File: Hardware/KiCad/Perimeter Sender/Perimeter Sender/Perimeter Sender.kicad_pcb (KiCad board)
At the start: 2 copper layers, 133.7 x 77.9 mm, 29 parts, among them J1 Conn_01x02, J2 Conn_01x02, J3 Conn_02x05_Row_Letter_Last, U1 AVR128DA48x-xPT, U2 INA233, U3 WeMos_D1_mini, U4 L298N, U5 TSR_1-2450, Y1 32.768kHz

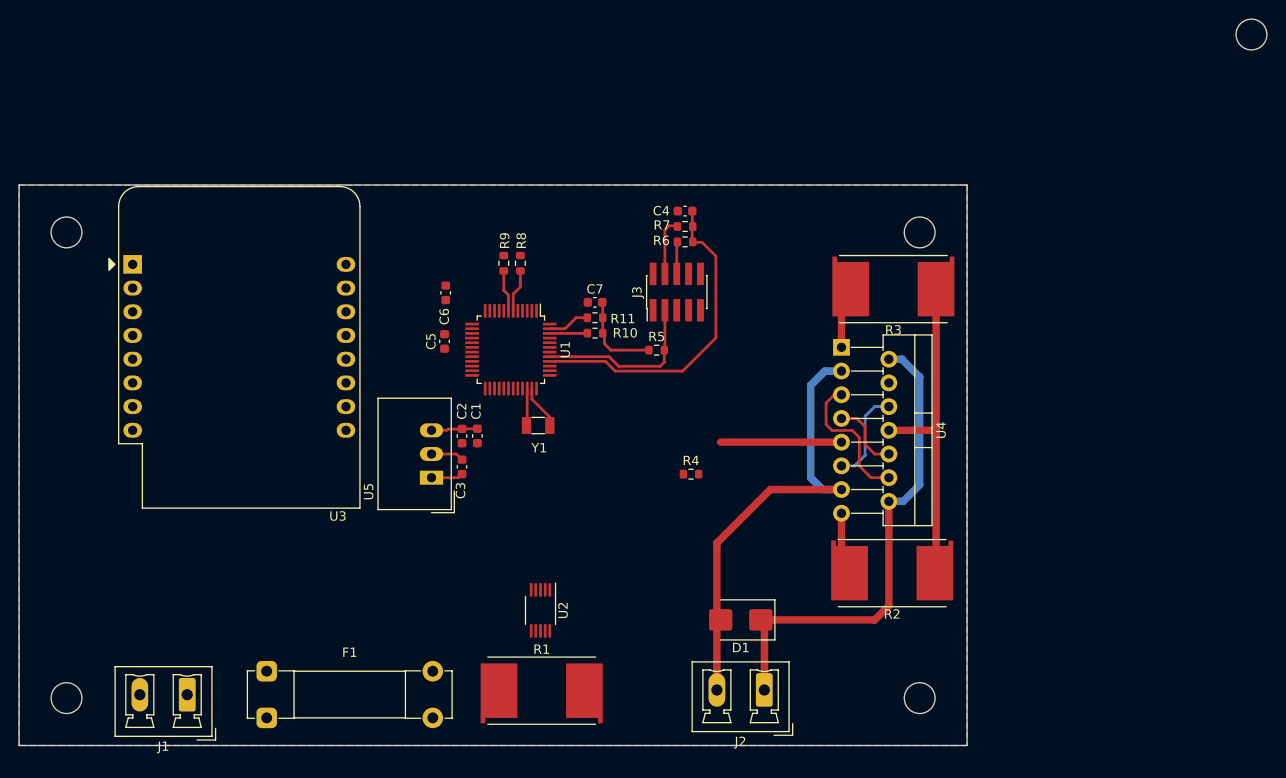
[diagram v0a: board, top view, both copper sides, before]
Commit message: Redesign: - Controller - I2C pinning geändert - uvm
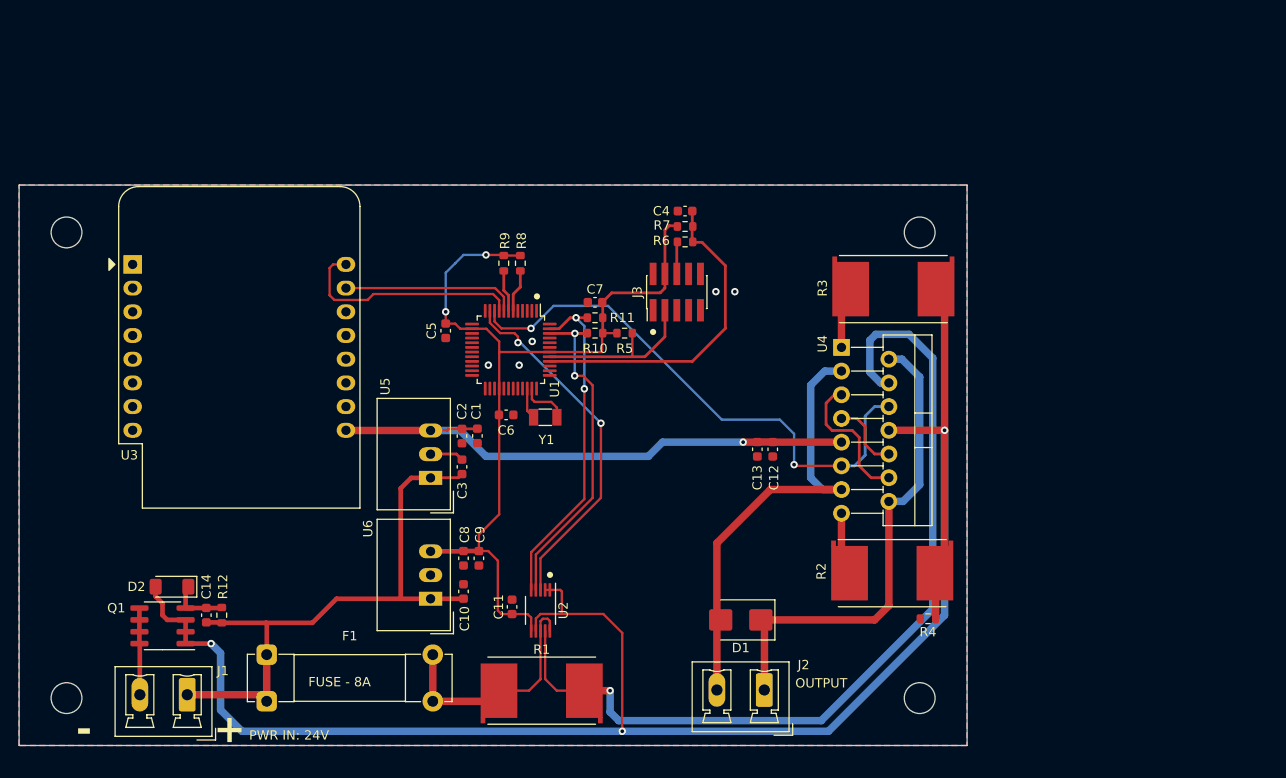
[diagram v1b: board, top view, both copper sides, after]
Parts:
- added C10: 100nF, Capacitor_SMD:C_0603_1608Metric, F.Cu at (111.1, 97.8)
- added C11: 100n, Capacitor_SMD:C_0603_1608Metric, F.Cu at (116.3, 99.4)
- added C12: 100n, Capacitor_SMD:C_0603_1608Metric, F.Cu at (144.3, 82.5)
- added C13: 1uF, Capacitor_SMD:C_0603_1608Metric, F.Cu at (142.6, 82.5)
- added C14: 1nF, Capacitor_SMD:C_0603_1608Metric, F.Cu at (83.6, 100.3)
- added C8: 100nF, Capacitor_SMD:C_0603_1608Metric, F.Cu at (111.1, 94.2)
- added C9: 4u7, Capacitor_SMD:C_0603_1608Metric, F.Cu at (112.8, 94.2)
- added D2: BZV55B10, Diode_SMD:D_MiniMELF, F.Cu at (79.9, 97.3)
- added Q1: Si4162DY, Package_SO:SOIC-8_3.9x4.9mm_P1.27mm, F.Cu at (78.9, 101.5)
- added R12: 10K, Resistor_SMD:R_0603_1608Metric, F.Cu at (85.2, 100.3)
- added U6: TSR_1-2433, Converter_DCDC:Converter_DCDC_TRACO_TSR-1_THT, F.Cu at (107.6, 98.6)
- moved R4 29.8 mm to (160.9, 100.7), turned to 180 degrees
- moved C6 14.6 mm to (115.7, 78.9), turned to 0 degrees
- moved R5 3.88 mm to (128.4, 70.1)
- moved F1 1.78 mm to (90.0, 104.6)
- moved Y1 1.17 mm to (119.9, 79.1)
- moved C5 1.15 mm to (109.2, 69.8), turned to -90 degrees
- moved U5 0.10 mm to (107.6, 85.6)
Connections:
- R2 pad 1: /POWER/POWER_IN_NEG -> /POWER/POWER_NEG
- R3 pad 1: /POWER/POWER_IN_NEG -> /POWER/POWER_NEG
- R4 pad 1: /POWER/POWER_IN_NEG -> /POWER/POWER_NEG
- U1 pad 14: Net-(U1-VDD-Pad14) -> +3.3V
- U1 pad 15: Net-(U1-GND-Pad15) -> GND
- U1 pad 28: unconnected-(U1-AVDD-Pad28) -> +3.3V
- U1 pad 29: Net-(U1-GND-Pad15) -> GND
- U1 pad 42: Net-(U1-VDD-Pad14) -> +3.3V
- U1 pad 43: Net-(U1-GND-Pad15) -> GND
- U2 pad 1: /POWER/POWER_IN_NEG -> /POWER/POWER_NEG
- U2 pad 2: /POWER/POWER_IN_NEG -> /POWER/POWER_NEG
- U2 pad 6: +5V -> +3.3V
- U2 pad 7: /POWER/POWER_IN_NEG -> /POWER/POWER_NEG
- U3 pad 10: unconnected-(U3-GND-Pad10) -> GND
- U3 pad 9: unconnected-(U3-5V-Pad9) -> +5V
- U4 pad 8: /POWER/POWER_IN_NEG -> /POWER/POWER_NEG
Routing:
- net /POWER/POWER_NEG: track 0.00 -> 190.9 mm, vias 0 -> 3
- net Net-(U2-Vin-): track 0.00 -> 95.7 mm, vias 0 -> 1
- net +3.3V: track 15.8 -> 95.4 mm, vias 0 -> 2
- net /POWER/POWER_IN_POS: track 3.43 -> 64.6 mm
- net /POWER_OUTPUT/EN: track 10.2 -> 58.8 mm, vias 0 -> 2
- net +5V: track 17.9 -> 59.9 mm, vias 0 -> 1
- net /POWER_OUTPUT//ALERT: track 0.00 -> 38.6 mm, vias 0 -> 2
- net /POWER_OUTPUT/SCL: track 4.52 -> 36.4 mm, vias 0 -> 2
- net /POWER_OUTPUT/SDA: track 4.04 -> 35.8 mm, vias 0 -> 2
- net /POWER/POWER_IN_NEG: track 35.8 -> 9.31 mm
- net Net-(U2-Vbus): track 0.00 -> 26.2 mm
- net /uC/UART_3_RXD: track 0.00 -> 24.9 mm
- net /uC/UART_3_TXD: track 0.00 -> 18.8 mm
- net Net-(D2-K): track 0.00 -> 6.31 mm
- net Net-(U1-XTAL32K1/PF0): track 4.00 -> 3.36 mm
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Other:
- board size 133.7 x 77.9 mm -> 101.6 x 60.1 mm
- board text added: "+"
- board text added: "-"
- board text added: "FUSE - 8A"
- board text added: "OUTPUT"
- board text added: "PWR IN: 24V"
